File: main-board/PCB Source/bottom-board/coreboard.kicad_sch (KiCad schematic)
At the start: 33 parts, among them J1 AS0A823-H4SB-7H, P8 SERIAL_DEBUG, U4 AT24CS08-STUM

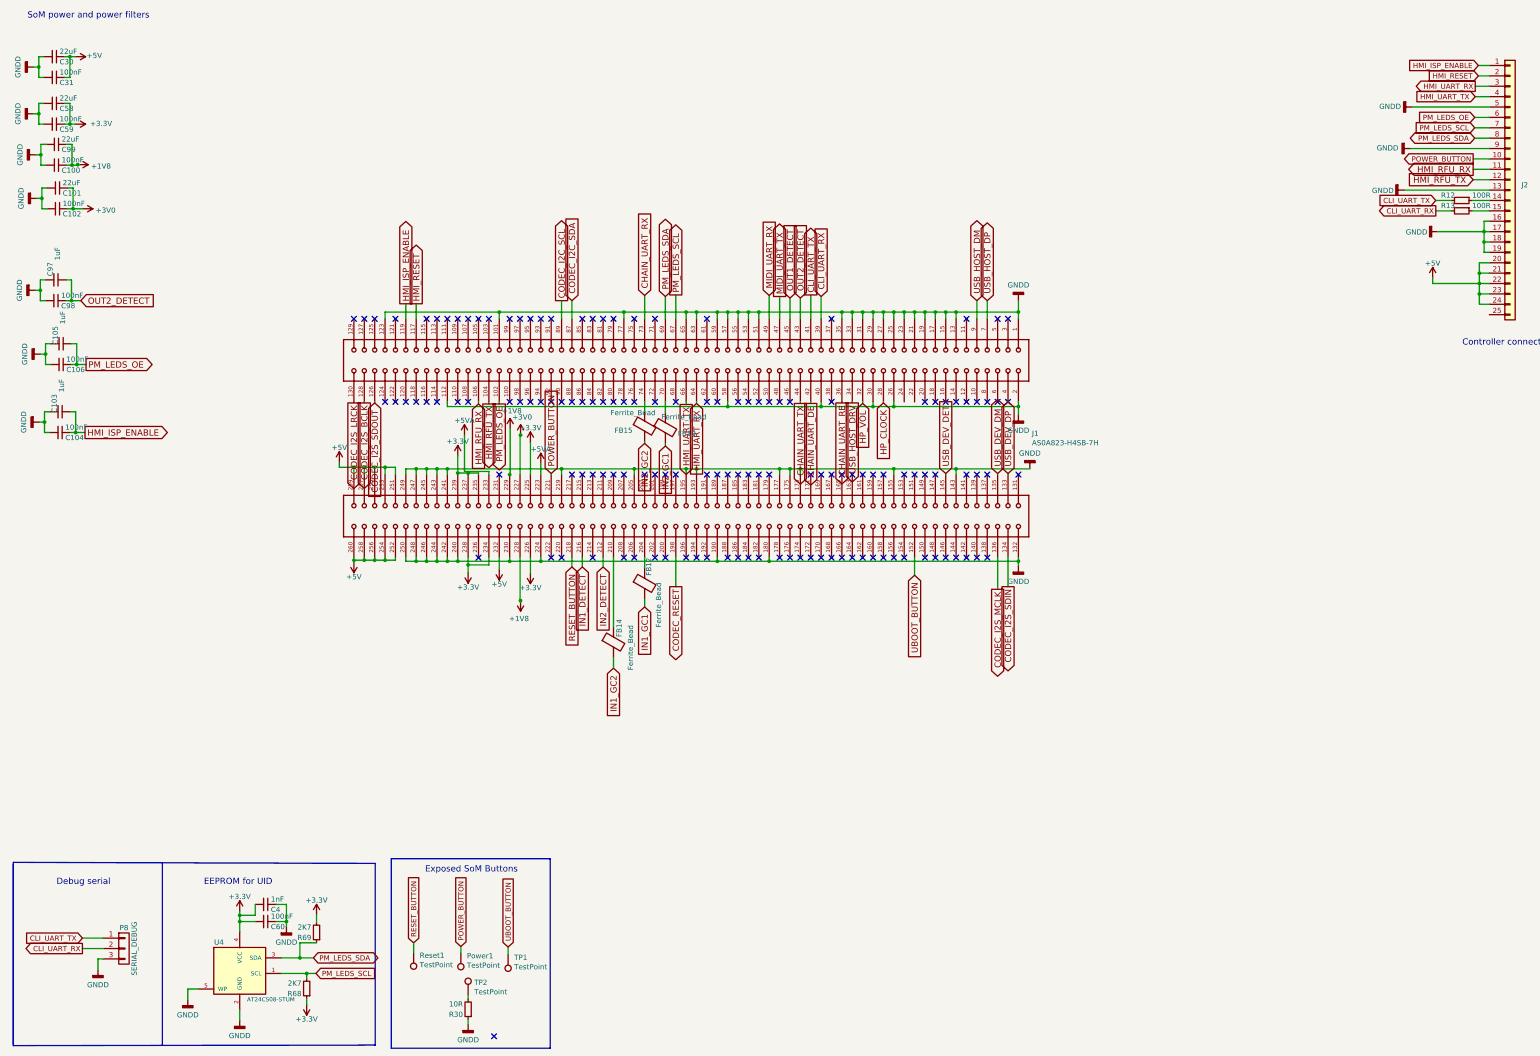
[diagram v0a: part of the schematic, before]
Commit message: mainboard: add bias buffer, update MPNs, clean schematic
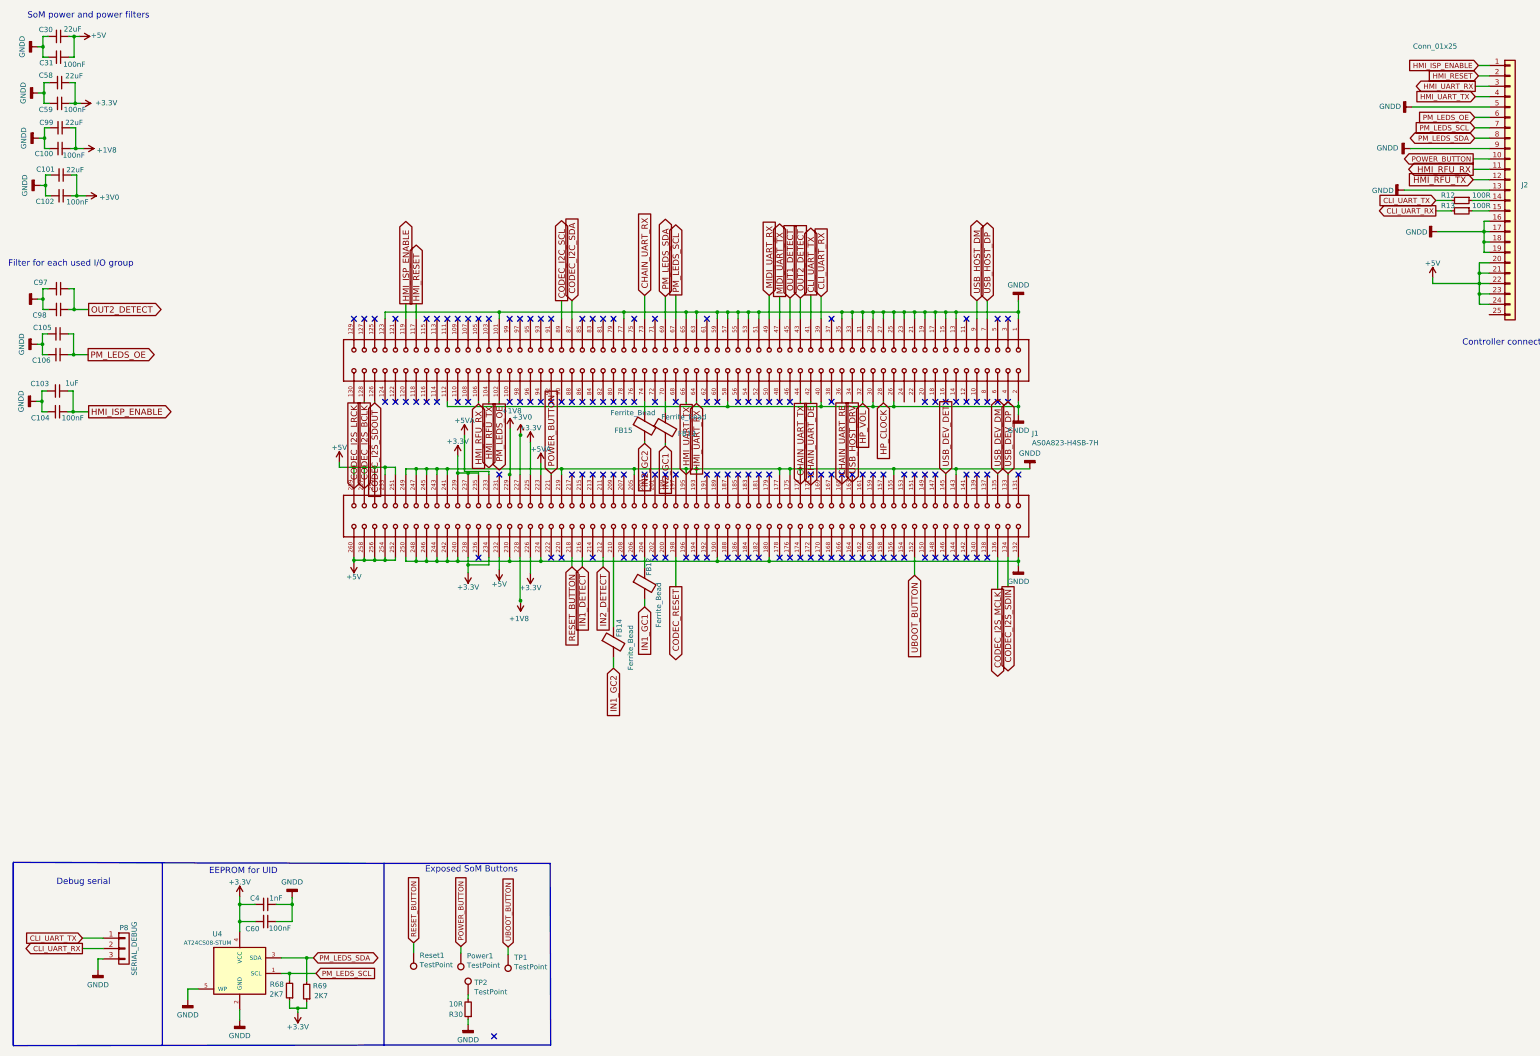
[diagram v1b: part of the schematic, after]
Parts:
- C105, C97: value 1uF -> (none); footprint Capacitor_SMD:C_0603_1608Metric -> (none)
- C106, C98: value 100nF -> (none); footprint Capacitor_SMD:C_0603_1608Metric -> (none)
- C4: MPN C0603X7R500-103KNP -> C0603X7R500-102KNP
- J2: value (none) -> Conn_01x25; footprint (none) -> F51L-1A7H1-11024:F51L-1A7H1-11024
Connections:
- net +3V3: now also R69.1; no longer R69.2
- net PM_LEDS_SDA: now also R69.2; no longer R69.1
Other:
- note added: "Filter for each used I/O group"
- moved on the sheet: C100, C101, C102, C103, C104, C105, C106, C30, C31, C58, C59, C99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

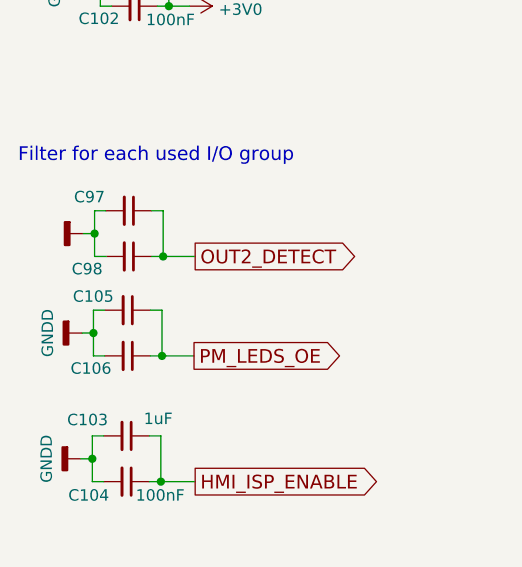
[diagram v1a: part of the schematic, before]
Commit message: mainboard: modify silkscreen
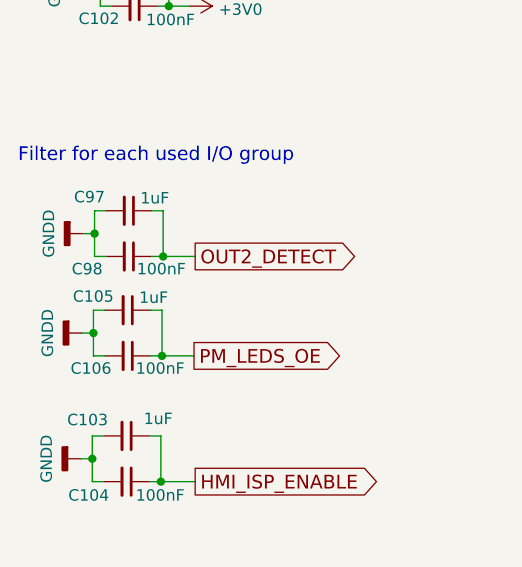
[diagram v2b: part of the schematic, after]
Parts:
- C105, C97: value (none) -> 1uF; footprint (none) -> Capacitor_SMD:C_0603_1608Metric
- C106, C98: value (none) -> 100nF; footprint (none) -> Capacitor_SMD:C_0603_1608Metric
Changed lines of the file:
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@@
       (effects (font (size 1.27 1.27)) (justify left))
     )
-    (property "Value" "" (id 1) (at 35.306 103.886 90)
-      (effects (font (size 1.27 1.27)) (justify left))
-    )
-    (property "Footprint" "" (id 2) (at 34.417 102.489 0)
+    (property "Value" "100nF" (id 1) (at 35.306 103.886 90)
+      (effects (font (size 1.27 1.27)) (justify left))
+    )
+    (property "Footprint" "Capacitor_SMD:C_0603_1608Metric" (id 2) (at 34.417 102.489 0)
       (effects (font (size 0 0)) hide)
     )
@@
       (effects (font (size 1.27 1.27)) (justify left))
     )
-    (property "Value" "" (id 1) (at 35.687 96.012 90)
-      (effects (font (size 1.27 1.27)) (justify left))
-    )
-    (property "Footprint" "" (id 2) (at 34.417 97.409 0)
+    (property "Value" "1uF" (id 1) (at 35.687 96.012 90)
+      (effects (font (size 1.27 1.27)) (justify left))
+    )
+    (property "Footprint" "Capacitor_SMD:C_0603_1608Metric" (id 2) (at 34.417 97.409 0)
       (effects (font (size 1.524 1.524)) hide)
     )
@@
       (effects (font (size 1.27 1.27)) (justify left))
     )
-    (property "Value" "" (id 1) (at 35.814 84.963 90)
-      (effects (font (size 1.27 1.27)) (justify left))
-    )
-    (property "Footprint" "" (id 2) (at 34.544 86.36 0)
+    (property "Value" "1uF" (id 1) (at 35.814 84.963 90)
+      (effects (font (size 1.27 1.27)) (justify left))
+    )
+    (property "Footprint" "Capacitor_SMD:C_0603_1608Metric" (id 2) (at 34.544 86.36 0)
       (effects (font (size 1.524 1.524)) hide)
     )
@@
       (effects (font (size 1.27 1.27)) (justify left))
     )
-    (property "Value" "" (id 1) (at 35.433 92.837 90)
-      (effects (font (size 1.27 1.27)) (justify left))
-    )
-    (property "Footprint" "" (id 2) (at 34.544 91.44 0)
+    (property "Value" "100nF" (id 1) (at 35.433 92.837 90)
+      (effects (font (size 1.27 1.27)) (justify left))
+    )
+    (property "Footprint" "Capacitor_SMD:C_0603_1608Metric" (id 2) (at 34.544 91.44 0)
       (effects (font (size 1.524 1.524)) hide)
     )
@@
       (effects (font (size 1.27 1.27)) hide)
     )
-    (property "Value" "" (id 1) (at 25.654 88.9 0))
+    (property "Value" "GNDD" (id 1) (at 25.654 88.9 0))
     (property "Footprint" "" (id 2) (at 29.464 88.9 0)
       (effects (font (size 1.524 1.524)))
